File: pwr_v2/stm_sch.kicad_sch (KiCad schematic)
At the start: 2 parts, among them CN11 Conn_02x36_Odd_Even, CN12 Conn_02x36_Odd_Even

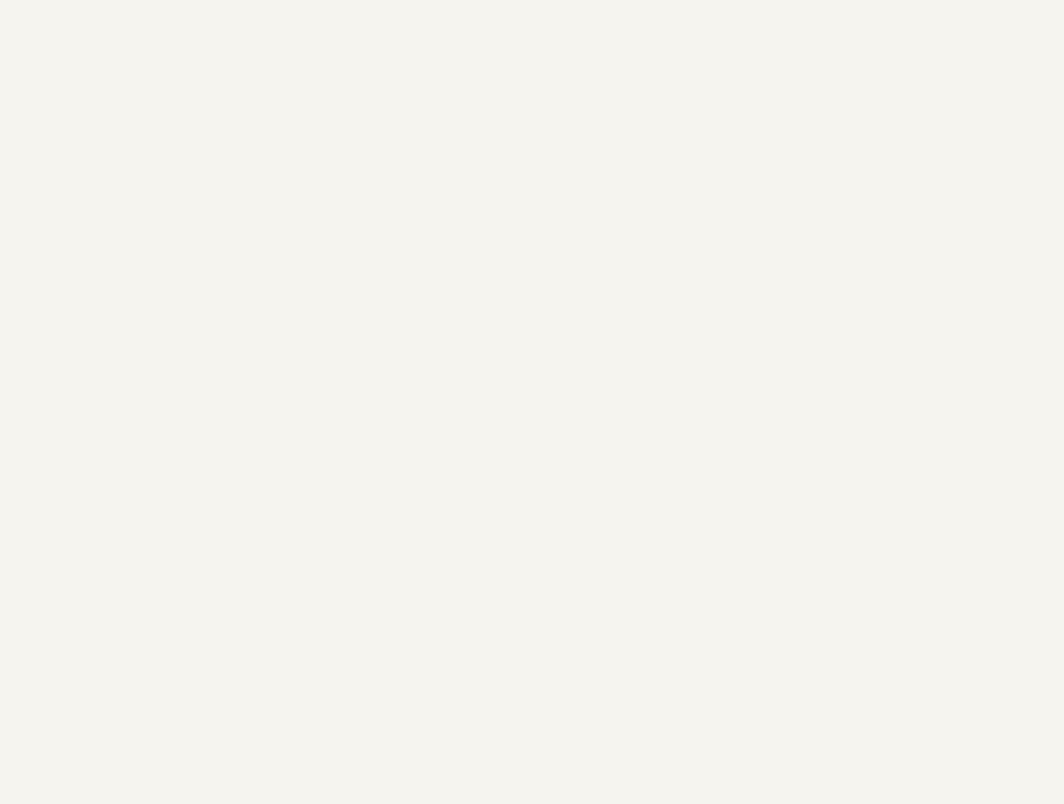
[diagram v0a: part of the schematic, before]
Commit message: File structure enhanced.
Added uniform titleblocks and 3D renders for easier view, file cleanups.
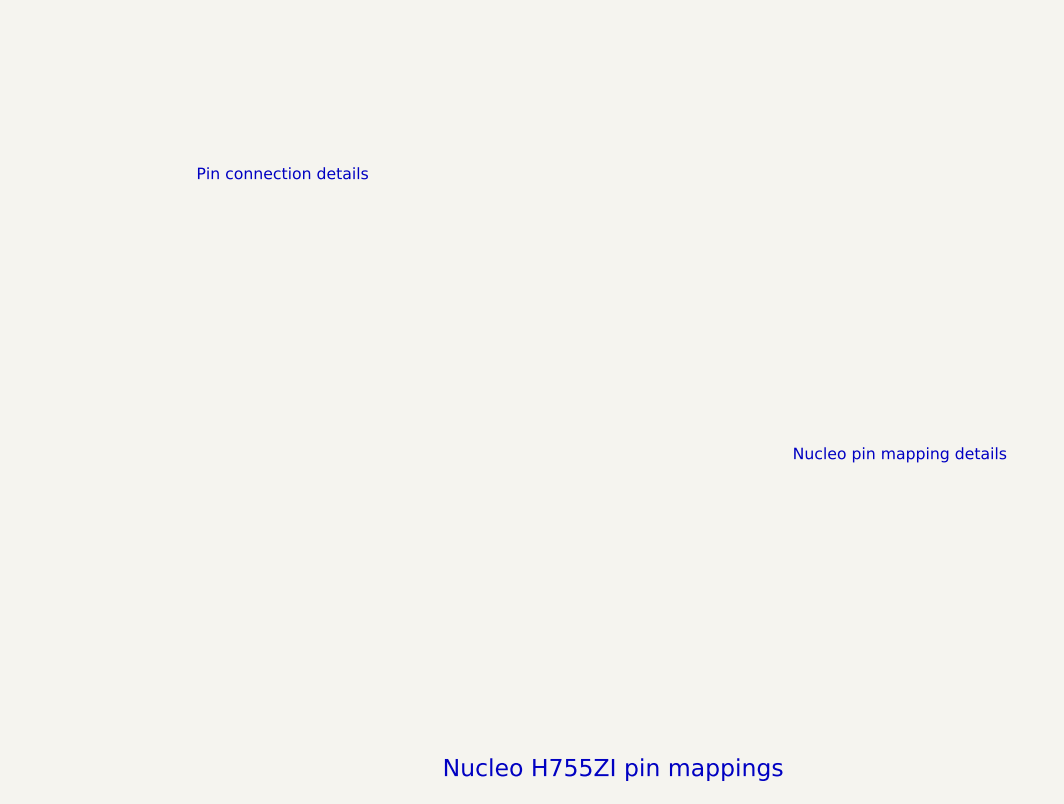
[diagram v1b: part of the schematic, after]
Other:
- note added: "Nucleo H755ZI pin mappings"
- note added: "Nucleo pin mapping details"
- note added: "Pin connection details"
- company: (none) -> Buck regulator circuits to generate 12V, 5V and 3.3V supplies.
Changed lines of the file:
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@@
 		(date "2025-05-11")
 		(rev "V2")
+		(company "Buck regulator circuits to generate 12V, 5V and 3.3V supplies.")
 		(comment 1 "STM32 headers")
 	)
+	(text "Pin connection details"
+		(exclude_from_sim no)
+		(at 178.435 103.505 0)
+		(effects
+			(font
+				(size 1.27 1.27)
+			)
+		)
+	)
+	(text "Nucleo H755ZI pin mappings"
+		(exclude_from_sim no)
+		(at 196.215 169.545 0)
+		(effects
+			(font
+				(size 1.905 1.905)
+			)
+			(justify left)
+		)
+	)
+	(text "Nucleo pin mapping details"
+		(exclude_from_sim no)
+		(at 247.015 134.62 0)
+		(effects
+			(font
+				(size 1.27 1.27)
+			)
+		)
+	)
 	(no_connect
 		(at 95.25 83.185)
@@
 			"////////////////////////////////////////////////////////////////////////////"
 			"////////////////////////////////////////////////////////////////////////////"
-			"/////////////////////////////////////////////////////w=="
+			"/////////////////////////////////////////////////////wAAAAAAAAAAAAAAAAAAAAAA"
+			"AAAAAAAAAAAAAAAAAAAAAAAAAAAAAAAAAAAAAAAAAAAAAAAAAAAAAAAAAAAAAAAAAAAAAAAAAAAA"
+			"AAAAAAAAAAAAAAAAAAAAAAAAAAAAAAAAAAAAAAAAAAAAAAAAAAAAAAAAAAAAAAAAAAAAAAAAAAAA"
+			"AAAAAAAAAAAAAAAAAAAAAAAAAAAAAAAAAAAAAAAAAAAAAAAAAAAAAAAAAAAAAAAAAAAAAAAAAAAA"
+			"AAAAAAAAAAAAAAAAAAAAAAAAAAAAAAAAAAAAAAAAAAAAAAAAAAAAAAAAAAAAAAAAAAAAAAAAAAAA"
+			"AAAAAAAAAAAAAAAAAAAAAAAAAAAAAAAAAAAAAAAAAAAAAAAAAAAAAAAAAAAAAAAAAAAAAAAAAAAA"
+			"AAAAAAAAAAAAAAAAAAAAAAAAAAAAAAAAAAAAAAAAAAAAAAAAAAAAAAAAAAAAAAAAAAAAAAAAAAAA"
+			"AAAAAAAAAAAAAAAAAAAAAAAAAAAAAAAAAAAAAAAAAAAAAAAAAAAAAAAAAAAAAAAAAAAAAAAAAAAA"
+			"AAAAAAAAAAAAAAAAAAAAAAAAAAAAAAAAAAAAAAAAAAAAAAAAAAAAAAAAAAAAAAAAAAAAAAAAAAAA"
+			"AAAAAAAAAAAAAAAAAAAAAAAAAAAAAAAAAAAAAAAAAAAAAAAAAAAAAAAAAAAAAAAAAAAAAAAAAAAA"
+			"AAAAAAAAAAAAAAAAAAAAAAAAAAAAAAAAAAAAAAAAAAAAAAAAAAAAAAAAAAAAAAAAAAAAAAAAAAAA"
+			"AAAAAAAAAAAAAAAAAAAAAAAAAAAAAAAAAAAAAAAAAAAAAAAAAAAAAAAAAAAAAAAAAAAAAAAAAAAA"
+			"AAAAAAAAAAAAAAAAAAAAAAAAAAAAAAAAAAAAAAAAAAAAAAAAAAAAAAAAAAAAAAAAAAAAAAAAAAAA"
+			"AAAAAAAAAAAAAAAAAAAAAAAAAAAAAAAAAAAAAAAAAAAAAAAAAAAAAAAAAAAAAAAAAAAAAAAAAAAA"
+			"AAAAAAAAAAAAAAAAAAAAAAAAAAAAAAAAAAAAAAAAAAAAAAAAAAAAAAAAAAAAAAAAAAAAAAAAAAAA"
+			"AAAAAAAAAAAAAAAAAAAAAAAAAAAAAAAAAAAAAAAAAAAAAAAAAAAAAAAAAAAAAAAAAAAAAAAAAAAA"
+			"AAAAAAAAAAAAAAAAAAAAAAAAAAAAAAAAAAAAAAAAAAAAAAAAAAAAAAAAAAAAAAAAAAAAAAAAAAAA"
+			"AAAAAAAAAAAAAAAAAAAAAAAAAAAAAAAAAAAAAAAAAAAAAAAAAAAAAAAAAAAAAAAAAAAAAAAAAAAA"
+			"AAAAAAAAAAAAAAAAAAAAAAAAAAAAAAAAAAAAAAAAAAAAAAAAAAAAAA=="
 		)
 	)
@@
 			"////////////////////////////////////////////////////////////////////////////"
 			"////////////////////////////////////////////////////////////////////////////"
-			"/////////////////////////////////////////////////w=="
+			"/////////////////////////////////////////////////wAAAAAAAAAAAAAAAAAAAAAAAAAA"
+			"AAAAAAAAAAAAAAAAAAAAAAAAAAAAAAAAAAAAAAAAAAAAAAAAAAAAAAAAAAAAAAAAAAAAAAAAAAAA"
+			"AAAAAAAAAAAAAAAAAAAAAAAAAAAAAAAAAAAAAAAAAAAAAAAAAAAAAAAAAAAAAAAAAAAAAAAAAAAA"
+			"AAAAAAAAAAAAAAAAAAAAAAAAAAAAAAAAAAAAAAAAAAAAAAAAAAAAAAAAAAAAAAAAAAAAAAAAAAAA"
+			"AAAAAAAAAAAAAAAAAAAAAAAAAAAAAAAAAAAAAAAAAAAAAAAAAAAAAAAAAAAAAAAAAAAAAAAAAAAA"
+			"AAAAAAAAAAAAAAAAAAAAAAAAAAAAAAAAAAAAAAAAAAAAAAAAAAAAAAAAAAAAAAAAAAAAAAAAAAAA"
+			"AAAAAAAAAAAAAAAAAAAAAAAAAAAAAAAAAAAAAAAAAAAAAAAAAAAAAAAAAAAAAAAAAAAAAAAAAAAA"
+			"AAAAAAAAAAAAAAAAAAAAAAAAAAAAAAAAAAAAAAAAAAAAAAAAAAAAAAAAAAAAAAAAAAAAAAAAAAAA"
+			"AAAAAAAAAAAAAAAAAAAAAAAAAAAAAAAAAAAAAAAAAAAAAAAAAAAAAAAAAAAAAAAAAAAAAAAAAAAA"
+			"AAAAAAAAAAAAAAAAAAAAAAAAAAAAAAAAAAAAAAAAAAAAAAAAAAAAAAAAAAAAAAAAAAAAAAAAAAAA"
+			"AAAAAAAAAAAAAAAAAAAAAAAAAAAAAAAAAAAAAAAAAAAAAAAAAAAAAAAAAAAAAAAAAAAAAAAAAAAA"
+			"AAAAAAAAAAAAAAAAAAAAAAAAAAAAAAAAAAAAAAAAAAAAAAAAAAAAAAAAAAAAAAAAAAAAAAAAAAAA"
+			"AAAAAAAAAAAAAAAAAAAAAAAAAAAAAAAAAAAAAAAAAAAAAAAAAAAAAAAAAAAAAAAAAAAAAAAAAAAA"
+			"AAAAAAAAAAAAAAAAAAAAAAAAAAAAAAAAAAAAAAAAAAAAAAAAAAAAAAAAAAAAAAAAAAAAAAAAAAAA"
+			"AAAAAAAAAAAAAAAAAAAAAAAAAAAAAAAAAAAAAAAAAAAAAAAAAAAAAAAAAAAAAAAAAAAAAAAAAAAA"
+			"AAAAAAAAAAAAAAAAAAAAAAAAAAAAAAAAAAAAAAAAAAAAAAAAAAAAAAAAAAAAAAAAAAAAAAAAAAAA"
+			"AAAAAAAAAAAAAAAAAAAAAAAAAAAAAAAAAAAAAAAAAAAAAAAAAAAAAAAAAAAAAAAAAAAAAAAAAAAA"
+			"AAAAAAAAAAAAAAAAAAAAAAAAAAAAAAAAAAAAAAAAAAAAAAAAAAAAAAAAAAAAAAAAAAAAAAAAAAAA"
+			"AAAAAAAAAAAAAAAAAAAAAAAAAAAAAAAAAAAAAAAAAAAAAAAAAA=="
 		)
 	)
@@
 			"AAAPAAAAAAAAAABtYWxsIEJvbGQAAAAAAAAAAAAAAAAAAA8AAAAAAAAAAGl0a2EgVGV4dAAAAAAA"
 			"AAAAAAAAAAAADwAAAAAAAAAAAAAAAAAAAAAAAAAAAAAAAAAAAAAAAAAAjJhhIgEAAAAAAAAAAAAA"
-			"AAAAAAAAAAAPAAAAAAAAAACVmGEiAQAAAAAAAAAAAAAAAAAAAAAAAA8AAAAAAAAAAGl0aw=="
+			"AAAAAAAAAAAPAAAAAAAAAACVmGEiAQAAAAAAAAAAAAAAAAAAAAAAAA8AAAAAAAAAAGl0awAAAAAA"
+			"AAAAAAAAAAAAAAAAAAAAAAAAAAAAAAAAAAAAAAAAAAAAAAAAAAAAAAAAAAAAAAAAAAAAAAAAAAAA"
+			"AAAAAAAAAAAAAAAAAAAAAAAAAAAAAAAAAAAAAAAAAAAAAAAAAAAAAAAAAAAAAAAAAAAAAAAAAAAA"
+			"AAAAAAAAAAAAAAAAAAAAAAAAAAAAAAAAAAAAAAAAAAAAAAAAAAAAAAAAAAAAAAAAAAAAAAAAAAAA"
+			"AAAAAAAAAAAAAAAAAAAAAAAAAAAAAAAAAAAAAAAAAAAAAAAAAAAAAAAAAAAAAAAAAAAAAAAAAAAA"
+			"AAAAAAAAAAAAAAAAAAAAAAAAAAAAAAAAAAAAAAAAAAAAAAAAAAAAAAAAAAAAAAAAAAAAAAAAAAAA"
+			"AAAAAAAAAAAAAAAAAAAAAAAAAAAAAAAAAAAAAAAAAAAAAAAAAAAAAAAAAAAAAAAAAAAAAAAAAAAA"
+			"AAAAAAAAAAAAAAAAAAAAAAAAAAAAAAAAAAAAAAAAAAAAAAAAAAAAAAAAAAAAAAAAAAAAAAAAAAAA"
+			"AAAAAAAAAAAAAAAAAAAAAAAAAAAAAAAAAAAAAAAAAAAAAAAAAAAAAAAAAAAAAAAAAAAAAAAAAAAA"
+			"AAAAAAAAAAAAAAAAAAAAAAAAAAAAAAAAAAAAAAAAAAAAAAAAAAAAAAAAAAAAAAAAAAAAAAAAAAAA"
+			"AAAAAAAAAAAAAAAAAAAAAAAAAAAAAAAAAAAAAAAAAAAAAAAAAAAAAAAAAAAAAAAAAAAAAAAAAAAA"
+			"AAAAAAAAAAAAAAAAAAAAAAAAAAAAAAAAAAAAAAAAAAAAAAAAAAAAAAAAAAAAAAAAAAAAAAAAAAAA"
+			"AAAAAAAAAAAAAAAAAAAAAAAAAAAAAAAAAAAAAAAAAAAAAAAAAAAAAAAAAAAAAAAAAAAAAAAAAAAA"
+			"AAAAAAAAAAAAAAAAAAAAAAAAAAAAAAAAAAAAAAAAAAAAAAAAAAAAAAAAAAAAAAAAAAAAAAAAAAAA"
+			"AAAAAAAAAAAAAAAAAAAAAAAAAAAAAAAAAAAAAAAAAAAAAAAAAAAAAAAAAAAAAAAAAAAAAAAAAAAA"
+			"AAAAAAAAAAAAAAAAAAAAAAAAAAAAAAAAAAAAAAAAAAAAAAAAAAAAAAAAAAAAAAAAAAAAAAAAAAAA"
+			"AAAAAAAAAAAAAAAAAAAAAAAAAAAAAAAAAAAAAAAAAAAAAAAAAAAAAAAAAAAAAAAAAAAAAAAAAAAA"
+			"AAAAAAAAAAAAAAAAAAAAAAAAAAAAAAAAAAAAAAAAAAAAAAAAAAAAAAAAAAAAAAAAAAAAAAAAAAAA"
+			"AAAAAAAAAAAAAAAAAAAAAAAAAAAAAAAAAAAAAAAAAAAAAAAAAAAAAAAAAAAAAAAAAAAAAA=="
 		)
 	)
